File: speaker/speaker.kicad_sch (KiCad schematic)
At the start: 33 parts, among them J2 JST Battery, J3 Speaker Output Pins, U1 PicoW, U2 MAX40203AUK+T, U3 MAX98357AETE_T, U4 MAX16054AZT_T

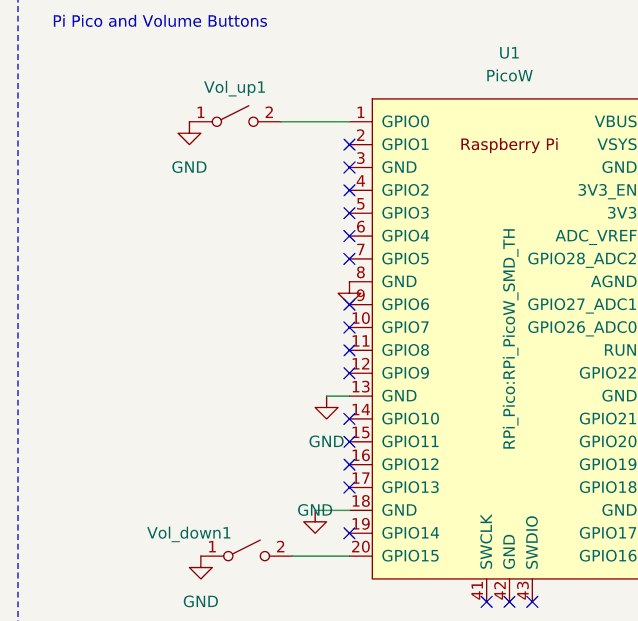
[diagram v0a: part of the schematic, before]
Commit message: add header
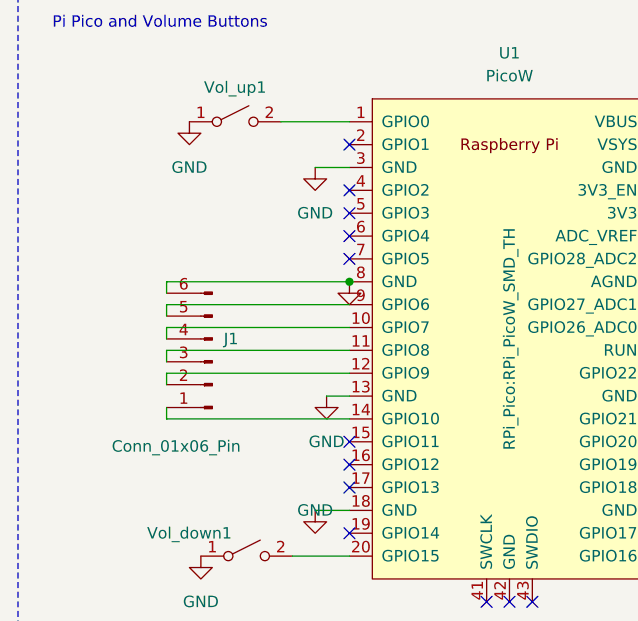
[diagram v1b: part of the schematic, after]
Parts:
- added J1: Conn_01x06_Pin, Connector_PinHeader_1.00mm:PinHeader_1x06_P1.00mm_Horizontal, symbol Connector:Conn_01x06_Pin
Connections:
- net GND: now also U1.3 (GND), J1.6 (Pin_6)
- net at U1.10 (GPIO7): now also J1.4 (Pin_4)
- net at U1.11 (GPIO8): now also J1.3 (Pin_3)
- net at U1.12 (GPIO9): now also J1.2 (Pin_2)
- net at U1.14 (GPIO10): now also J1.1 (Pin_1)
- net at U1.9 (GPIO6): now also J1.5 (Pin_5)
- no-connect marks 29 -> 23

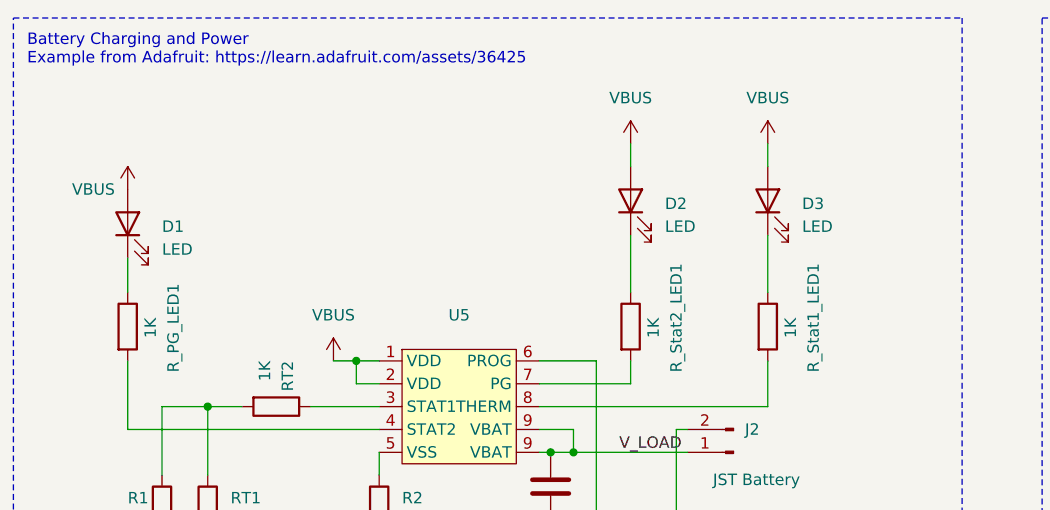
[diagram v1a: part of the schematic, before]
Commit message: Update speaker.kicad_sch
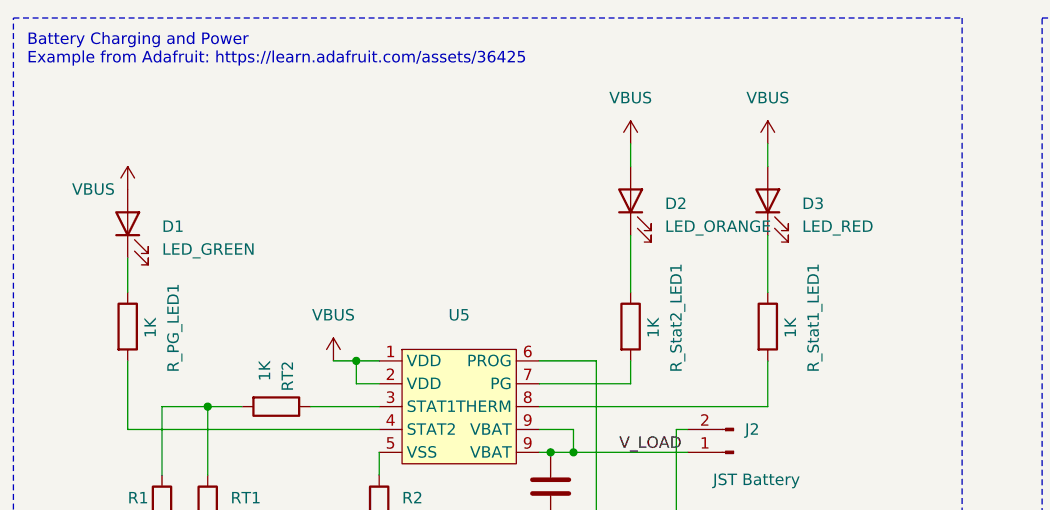
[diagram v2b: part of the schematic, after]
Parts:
- D1: value LED -> LED_GREEN
- D2: value LED -> LED_ORANGE
- D3: value LED -> LED_RED
- R1, R2: MPN (none) -> ERJ-3EKF2001V
- R3: MPN (none) -> ERJ-3EKF1004V
- R4: MPN (none) -> RC0603FR-0710KL
- R5, R6: MPN (none) -> ERJ-3EKF2002V
- RT1: Link (none) -> https://www.digikey.com/en/products/detail/yageo/RC0603FR-0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; MPN (none) -> RC0603FR-07150KL
- RT2, R_PG_LED1, R_Stat1_LED1, R_Stat2_LED1: Link (none) -> https://www.digikey.com/en/products/detail/yageo/RC0603FR-0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; MPN (none) -> RC0603FR-071KL
- U2: Link (none) -> https://www.digikey.com/en/products/detail/analog-devices-i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; MPN (none) -> MAX40203AUK+T
- U3: Link (none) -> https://www.digikey.com/en/products/detail/analog-devices-i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; MPN (none) -> MAX98357AETE_T
- U4: Link (none) -> https://www.digikey.com/en/products/detail/analog-devices-i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; MPN (none) -> MAX16054AZT_T
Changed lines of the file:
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@@
 			)
 		)
-		(property "Link" ""
+		(property "Link" "https://www.digikey.com/en/products/detail/yageo/RC0603FR-07150KL/726959"
+			(at 39.37 71.12 0)
+			(effects
+				(font
+					(size 1.27 1.27)
+				)
+				(hide yes)
+			)
+		)
+		(property "MPN" "RC0603FR-07150KL"
 			(at 39.37 71.12 0)
 			(effects
@@
 			)
 		)
-		(property "Link" ""
+		(property "Link" "https://www.digikey.com/en/products/detail/yageo/RC0603FR-071KL/726843"
+			(at 101.6 50.8 0)
+			(effects
+				(font
+					(size 1.27 1.27)
+				)
+				(hide yes)
+			)
+		)
+		(property "MPN" "RC0603FR-071KL"
 			(at 101.6 50.8 0)
 			(effects
@@
 			)
 		)
-		(property "Link" ""
+		(property "Link" "https://www.digikey.com/en/products/detail/analog-devices-inc-maxim-integrated/MAX40203AUK-T/10447227?msockid=1cfcdfe0f76b64111d36cc60f6416529"
+			(at 209.55 40.64 0)
+			(effects
+				(font
+					(size 1.27 1.27)
+				)
+				(hide yes)
+			)
+		)
+		(property "MPN" "MAX40203AUK+T"
 			(at 209.55 40.64 0)
 			(effects
@@
 		(fields_autoplaced yes)
 		(property "Reference" "D1"
-			(at 34.29 39.6875 90)
+			(at 34.29 39.6874 90)
 			(effects
 				(font
@@
 			)
 		)
-		(property "Value" "LED"
-			(at 34.29 42.2275 90)
+		(property "Value" "LED_GREEN"
+			(at 34.29 42.2274 90)
 			(effects
 				(font
@@
 			)
 		)
+		(property "MPN" "ERJ-3EKF2002V"
+			(at 255.27 49.53 0)
+			(effects
+				(font
+					(size 1.27 1.27)
+				)
+				(hide yes)
+			)
+		)
 		(pin "2"
 		)
@@
 			)
 		)
-		(property "Link" ""
+		(property "Link" "https://www.digikey.com/en/products/detail/yageo/RC0603FR-071KL/726843"
+			(at 86.36 50.8 0)
+			(effects
+				(font
+					(size 1.27 1.27)
+				)
+				(hide yes)
+			)
+		)
+		(property "MPN" "RC0603FR-071KL"
 			(at 86.36 50.8 0)
 			(effects
@@
 		(fields_autoplaced yes)
 		(property "Reference" "D2"
-			(at 90.17 37.1475 90)
+			(at 90.17 37.1474 90)
 			(effects
 				(font
@@
 			)
 		)
-		(property "Value" "LED"
-			(at 90.17 39.6875 90)
+		(property "Value" "LED_ORANGE"
+			(at 90.17 39.6874 90)
 			(effects
 				(font
@@
 			)
 		)
+		(property "MPN" "ERJ-3EKF2002V"
+			(at 104.14 129.54 0)
+			(effects
+				(font
+					(size 1.27 1.27)
+				)
+				(hide yes)
+			)
+		)
 		(pin "2"
 		)
@@
 			)
 		)
+		(property "MPN" "ERJ-3EKF2001V"
+			(at 34.29 71.12 0)
+			(effects
+				(font
+					(size 1.27 1.27)
+				)
+				(hide yes)
+			)
+		)
 		(pin "1"
 		)
@@
 			)
 		)
+		(property "MPN" "ERJ-3EKF2001V"
+			(at 58.42 71.12 0)
+			(effects
+				(font
+					(size 1.27 1.27)
+				)
+				(hide yes)
+			)
+		)
 		(pin "1"
 		)
@@
 			)
 		)
-		(property "Link" ""
+		(property "Link" "https://www.digikey.com/en/products/detail/yageo/RC0603FR-071KL/726843"
+			(at 30.48 50.8 0)
+			(effects
+				(font
+					(size 1.27 1.27)
+				)
+				(hide yes)
+			)
+		)
+		(property "MPN" "RC0603FR-071KL"
 			(at 30.48 50.8 0)
 			(effects
@@
 			)
 		)
-		(property "Link" ""
+		(property "Link" "https://www.digikey.com/en/products/detail/analog-devices-inc-maxim-integrated/MAX16054AZT-T/1938114?msockid=1cfcdfe0f76b64111d36cc60f6416529"
+			(at 167.64 50.8 0)
+			(effects
+				(font
+					(size 1.27 1.27)
+				)
+				(hide yes)
+			)
+		)
+		(property "MPN" "MAX16054AZT_T"
 			(at 167.64 50.8 0)
 			(effects
@@
 			)
 		)
-		(property "MPN" ""
+		(property "MPN" "MAX98357AETE_T"
 			(at 193.04 124.46 0)
 			(effects
@@
 			)
 		)
-		(property "Link" ""
+		(property "Link" "https://www.digikey.com/en/products/detail/analog-devices-inc-maxim-integrated/MAX16054AZT-T/1938114?msockid=1cfcdfe0f76b64111d36cc60f6416529"
 			(at 193.04 124.46 0)
 			(effects
@@
 		(fields_autoplaced yes)
 		(property "Reference" "D3"
-			(at 105.41 37.1475 90)
+			(at 105.41 37.1474 90)
 			(effects
 				(font
@@
 			)
 		)
-		(property "Value" "LED"
-			(at 105.41 39.6875 90)
+		(property "Value" "LED_RED"
+			(at 105.41 39.6874 90)
 			(effects
 				(font
@@
 			)
 		)
+		(property "MPN" "ERJ-3EKF1004V"
+			(at 214.63 116.84 0)
+			(effects
+				(font
+					(size 1.27 1.27)
+				)
+				(hide yes)
+			)
+		)
 		(pin "1"
 		)
@@
 			)
 		)
+		(property "MPN" "RC0603FR-0710KL"
+			(at 193.04 49.53 0)
+			(effects
+				(font
+					(size 1.27 1.27)
+				)
+				(hide yes)
+			)
+		)
 		(pin "2"
 		)
@@
 			)
 		)
-		(property "Link" ""
+		(property "Link" "https://www.digikey.com/en/products/detail/yageo/RC0603FR-071KL/726843"
+			(at 46.99 59.69 0)
+			(effects
+				(font
+					(size 1.27 1.27)
+				)
+				(hide yes)
+			)
+		)
+		(property "MPN" "RC0603FR-071KL"
 			(at 46.99 59.69 0)
 			(effects

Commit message: update bom
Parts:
- C1, C5: MPN (none) -> 0603B221K500CT
- C2, C3: MPN (none) -> CL10A106MQ8NNNC
- C4: MPN (none) -> CC0603KRX7R7BB104
- D1: MPN (none) -> 150040GS73240
- D2: MPN (none) -> SML-LX0402SOC-TR
- D3: MPN (none) -> XZMDK68W-2
- H1, H2, H3, H4, J1, J2, J3, On_Off1, U1, Vol_down1, Vol_up1: now not fitted
- U5: value ~ -> MCP73833; MPN (none) -> MCP73833-CNI/UN
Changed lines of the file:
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@@
 			)
 		)
+		(property "MPN" "CC0603KRX7R7BB104"
+			(at 167.64 152.4 0)
+			(effects
+				(font
+					(size 1.27 1.27)
+				)
+				(hide yes)
+			)
+		)
 		(pin "1"
 		)
@@
 		(in_bom yes)
 		(on_board yes)
-		(dnp no)
+		(dnp yes)
 		(property "Reference" "On_Off1"
 			(at 140.97 41.91 0)
@@
 			)
 		)
+		(property "MPN" "150040GS73240"
+			(at 30.48 39.37 0)
+			(effects
+				(font
+					(size 1.27 1.27)
+				)
+				(hide yes)
+			)
+		)
 		(pin "1"
 		)
@@
 		(in_bom yes)
 		(on_board yes)
-		(dnp no)
+		(dnp yes)
 		(fields_autoplaced yes)
 		(property "Reference" "H4"
@@
 		(in_bom yes)
 		(on_board yes)
-		(dnp no)
+		(dnp yes)
 		(property "Reference" "Vol_down1"
 			(at 36.83 163.83 0)
@@
 			)
 		)
+		(property "MPN" "SML-LX0402SOC-TR"
+			(at 86.36 36.83 0)
+			(effects
+				(font
+					(size 1.27 1.27)
+				)
+				(hide yes)
+			)
+		)
 		(pin "1"
 		)
@@
 		(in_bom yes)
 		(on_board yes)
-		(dnp no)
+		(dnp yes)
 		(property "Reference" "J2"
 			(at 99.06 62.23 0)
@@
 		(in_bom yes)
 		(on_board yes)
-		(dnp no)
+		(dnp yes)
 		(property "Reference" "Vol_up1"
 			(at 41.91 114.3 0)
@@
 		(in_bom yes)
 		(on_board yes)
-		(dnp no)
+		(dnp yes)
 		(fields_autoplaced yes)
 		(property "Reference" "H1"
@@
 			)
 		)
+		(property "MPN" "0603B221K500CT"
+			(at 156.21 130.81 0)
+			(effects
+				(font
+					(size 1.27 1.27)
+				)
+				(hide yes)
+			)
+		)
 		(pin "1"
 		)
@@
 		(in_bom yes)
 		(on_board yes)
-		(dnp no)
+		(dnp yes)
 		(fields_autoplaced yes)
 		(property "Reference" "H2"
@@
 			)
 		)
+		(property "MPN" "XZMDK68W-2"
+			(at 101.6 36.83 0)
+			(effects
+				(font
+					(size 1.27 1.27)
+				)
+				(hide yes)
+			)
+		)
 		(pin "1"
 		)
@@
 		(in_bom yes)
 		(on_board yes)
-		(dnp no)
+		(dnp yes)
 		(property "Reference" "J1"
 			(at 40.64 142.2399 0)
@@
 			)
 		)
+		(property "MPN" "CL10A106MQ8NNNC"
+			(at 77.47 68.58 0)
+			(effects
+				(font
+					(size 1.27 1.27)
+				)
+				(hide yes)
+			)
+		)
 		(pin "1"
 		)
@@
 		(in_bom yes)
 		(on_board yes)
-		(dnp no)
+		(dnp yes)
 		(fields_autoplaced yes)
 		(property "Reference" "H3"
@@
 		(in_bom yes)
 		(on_board yes)
-		(dnp no)
+		(dnp yes)
 		(property "Reference" "J3"
 			(at 143.51 127 0)
@@
 			)
 		)
+		(property "MPN" "0603B221K500CT"
+			(at 166.37 133.35 0)
+			(effects
+				(font
+					(size 1.27 1.27)
+				)
+				(hide yes)
+			)
+		)
 		(pin "2"
 		)
@@
 			)
 		)
+		(property "MPN" "CL10A106MQ8NNNC"
+			(at 160.02 152.4 0)
+			(effects
+				(font
+					(size 1.27 1.27)
+				)
+				(hide yes)
+			)
+		)
 		(pin "1"
 		)
@@
 			)
 		)
-		(property "Value" "~"
+		(property "Value" "MCP73833"
 			(at 67.31 52.07 0)
 			(effects
@@
 			)
 		)
+		(property "MPN" "MCP73833-CNI/UN"
+			(at 66.04 59.69 0)
+			(effects
+				(font
+					(size 1.27 1.27)
+				)
+				(hide yes)
+			)
+		)
 		(pin "1"
 		)
@@
 		(in_bom yes)
 		(on_board yes)
-		(dnp no)
+		(dnp yes)
 		(fields_autoplaced yes)
 		(property "Reference" "U1"

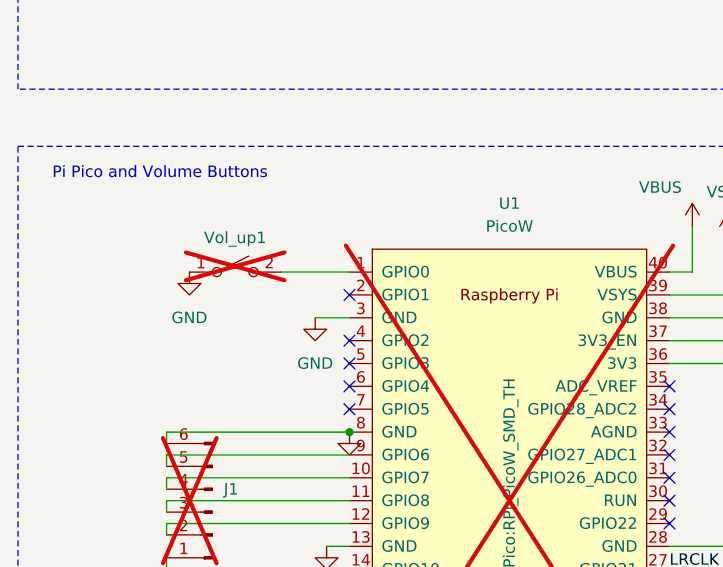
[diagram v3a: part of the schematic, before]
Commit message: update schematic
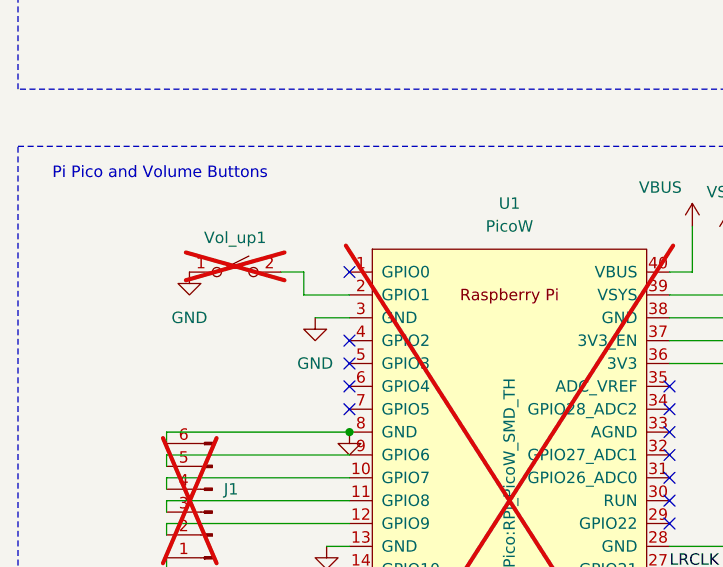
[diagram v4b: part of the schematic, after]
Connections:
- net at Vol_up1.2 (B): now also U1.2 (GPIO1); no longer U1.1 (GPIO0)
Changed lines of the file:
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@@
-	)
-	(no_connect
-		(at 54.61 120.65)
 	)
 	(no_connect
@@
 	)
 	(no_connect
+		(at 54.61 118.11)
+	)
+	(no_connect
 		(at 90.17 143.51)
 	)
@@
 	(wire
 		(pts
+			(xy 49.53 118.11) (xy 49.53 120.65)
+		)
+		(stroke
+			(width 0)
+			(type default)
+		)
+	)
+	(wire
+		(pts
 			(xy 76.2 62.23) (xy 80.01 62.23)
 		)
@@
 	(wire
 		(pts
+			(xy 49.53 120.65) (xy 54.61 120.65)
+		)
+		(stroke
+			(width 0)
+			(type default)
+		)
+	)
+	(wire
+		(pts
 			(xy 76.2 54.61) (xy 82.55 54.61)
 		)
@@
 	(wire
 		(pts
-			(xy 46.99 118.11) (xy 54.61 118.11)
-		)
-		(stroke
-			(width 0)
-			(type default)
-		)
-	)
-	(wire
-		(pts
 			(xy 198.12 59.69) (xy 250.19 59.69)
 		)
@@
 		)
 		(stroke
+			(width 0)
+			(type default)
+		)
+	)
+	(wire
+		(pts
+			(xy 46.99 118.11) (xy 49.53 118.11)
+		)
+		(stroke

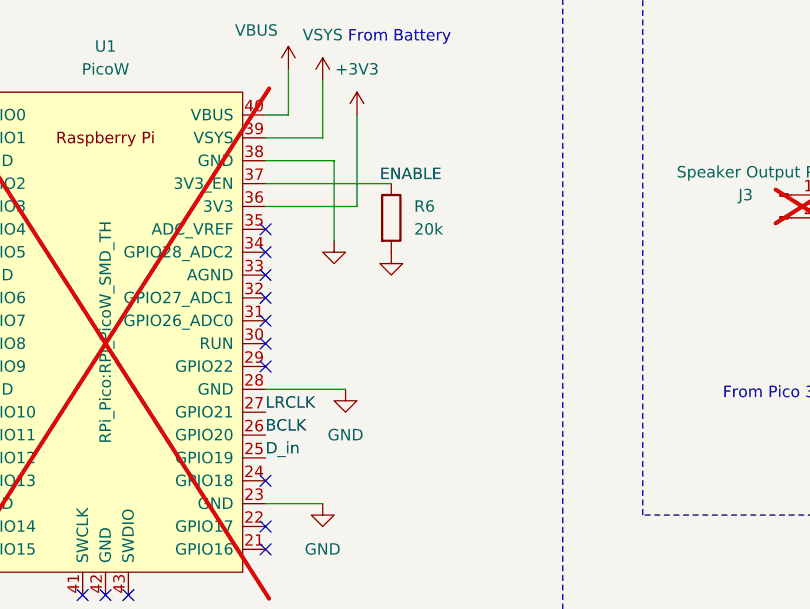
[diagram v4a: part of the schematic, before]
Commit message: changed footprint for battery connector
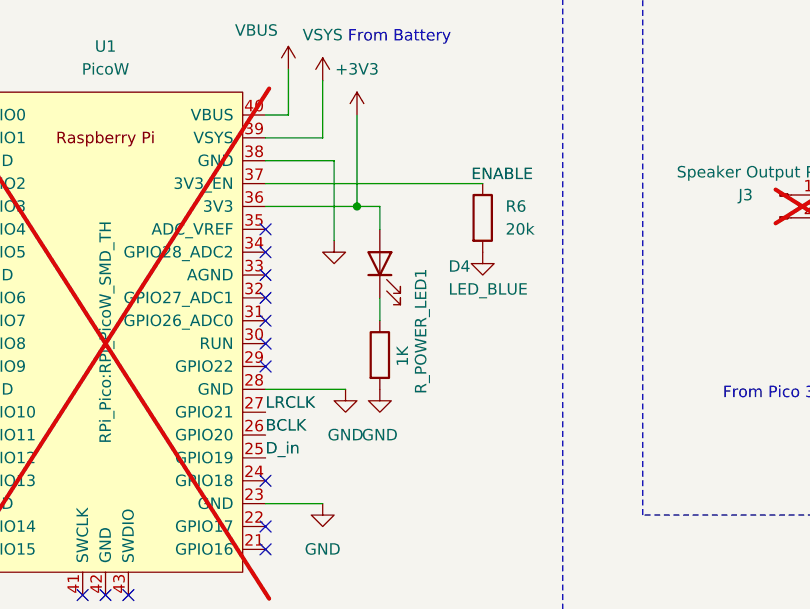
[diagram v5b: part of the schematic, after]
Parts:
- added D4: LED_BLUE, LED_SMD:LED_0402_1005Metric_Pad0.77x0.64mm_HandSolder, symbol Device:LED
- added R_POWER_LED1: 1K, Resistor_SMD:R_0603_1608Metric, symbol Device:R
- J2: footprint Connector_JST:JST_PH_S2B-PH-K_1x02_P2.00mm_Horizontal -> Connector_JST:JST_PH_S2B-PH-SM4-TB_1x02-1MP_P2.00mm_Horizontal
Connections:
- net +3V3: now also D4.2 (A)
- net GND: now also R_POWER_LED1.2
- new net: D4.1 (K), R_POWER_LED1.1
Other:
- moved on the sheet: R6
